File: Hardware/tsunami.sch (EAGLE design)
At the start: 154 parts, among them J1 VDC-IN, J10 TRIG2, J11 TRIG1, J12 USD-SDIO-SOCKET, J13 GND, J14 AUDIO I/O, J15 MIDI, J2 GND-IN, J3 DEBUG, J4 USB-MICROB", J5 CORTEX_DEBUGPTH, J6 3.3VA, J7 3.3V, J8 !PLAYING, J9 FTDI_DEVICE, Q1 2.5A/30V, U1 LM1117, U2 LM1117, U3 ATSAMS70NXXA-AN, U4 AK4618VQSFE-PACKAGE, U5 74AHC1G125, U6 6N138M, Y1 11.2896 MHz

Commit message: Updates from reviews.
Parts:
- added TP5: SWDIO/TMS, SparkFun-Passives:TEST-POINTTP_15TH_THRU
- added TP6: SWCK/TCK, SparkFun-Passives:TEST-POINTTP_15TH_THRU
- added TP7: TDO, SparkFun-Passives:TEST-POINTTP_15TH_THRU
- added TP8: TDI, SparkFun-Passives:TEST-POINTTP_15TH_THRU
- added TP9: NRESET, SparkFun-Passives:TEST-POINTTP_15TH_THRU
- U3: value ATSAMS70NXXA-AN -> ATSAMS70N20A-AN
- renumbered L2 to FB1, L3 to FB2, L4 to FB3
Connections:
- net 3.3V_A renamed VCCA
- net N$7 renamed VBUS
- new net SHIELD: J4.SHIELD
- net NRESET: now also TP9.1
- net SWCLK/TCK: now also TP6.1
- net SWDIO/TMS: now also TP5.1
- net TDI: now also TP8.1
- net TDO: now also TP7.1
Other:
- note added: "Highpass filters with 1.59 Hz cutoff."
- note added: "Lowpass filters with 159 kHz cutoff."
- note added: "Power inputs prioritize header over USB. If 5V is present on both, current is drawn from header."
- note removed: "Power inputs prioritize header over USB. If 5V is present on both, current is drawn from barrel."
- moved on the sheet: D1, J3, J4, J5, R10, R5, R6, R9

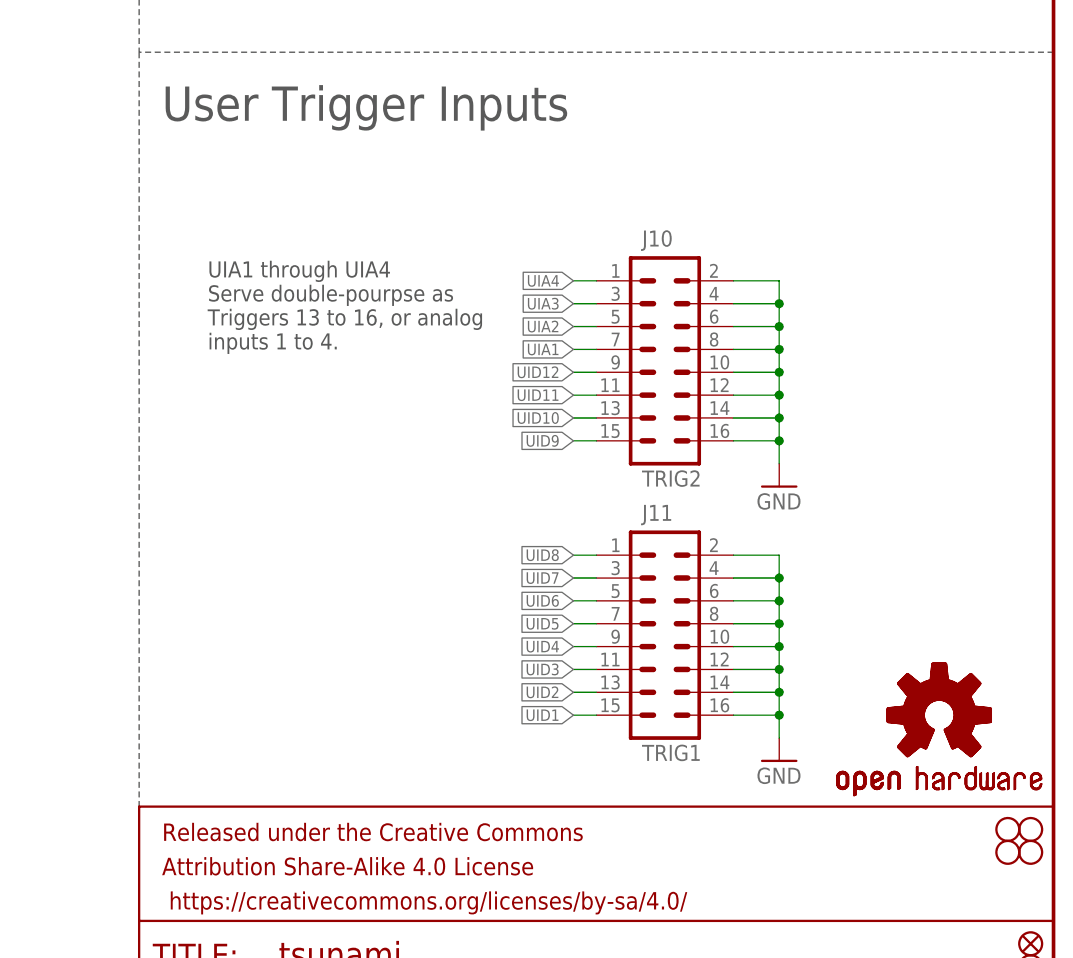
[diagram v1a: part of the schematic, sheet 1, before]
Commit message: Some checklist touchups
JTAG TP's placed on 50 mil grid.
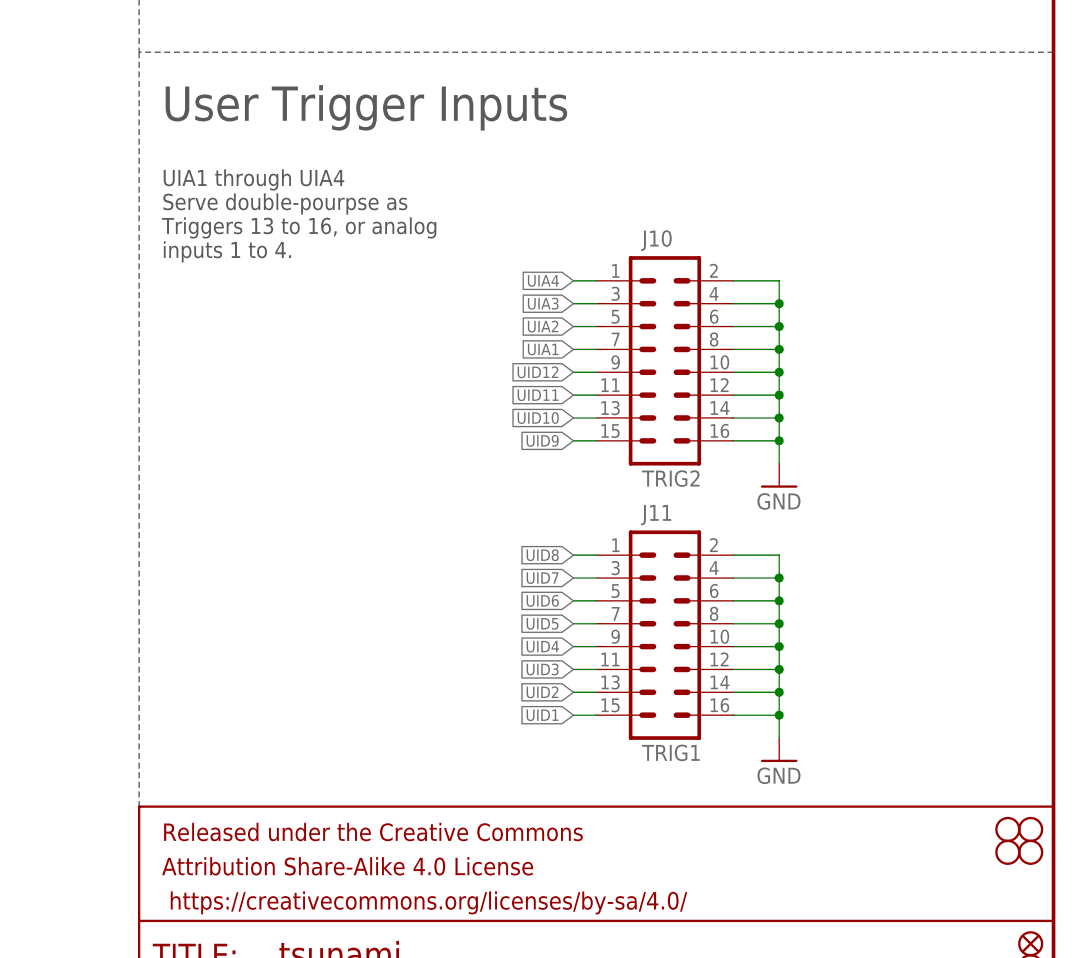
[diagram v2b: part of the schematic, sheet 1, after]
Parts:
- removed LOGO2, LOGO3: OSHW-LOGOM, SparkFun-Aesthetics:OSHW-LOGOM
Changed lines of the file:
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@@
 <part name="FD1" library="SparkFun-Aesthetics" deviceset="FIDUCIAL" device="UFIDUCIAL"/>
 <part name="FD2" library="SparkFun-Aesthetics" deviceset="FIDUCIAL" device="UFIDUCIAL"/>
-<part name="LOGO3" library="SparkFun-Aesthetics" deviceset="OSHW-LOGO" device="M"/>
 <part name="LOGO1" library="SparkFun-Aesthetics" deviceset="SFE_LOGO_NAME" device=".2_INCH"/>
 <part name="Q1" library="SparkFun-DiscreteSemi" deviceset="MOSFET-PCHANNEL" device="DMG2307L" value="2.5A/30V"/>
@@
 <part name="J1" library="SparkFun-Connectors" deviceset="M02" device="PTH" value="VDC-IN"/>
 <part name="J2" library="SparkFun-Connectors" deviceset="M02" device="PTH" value="GND-IN"/>
-<part name="LOGO2" library="SparkFun-Aesthetics" deviceset="OSHW-LOGO" device="M"/>
 <part name="U$1" library="SparkFun-Aesthetics" deviceset="VCCA" device=""/>
 <part name="U$2" library="SparkFun-Aesthetics" deviceset="VCCA" device=""/>
@@
 <wire x1="63.5" y1="58.42" x2="119.38" y2="58.42" width="0.1524" layer="97" style="shortdash"/>
 <wire x1="330.2" y1="279.4" x2="330.2" y2="215.9" width="0.1524" layer="97" style="shortdash"/>
-<text x="337.82" y="86.36" size="1.778" layer="97" font="vector">UIA1 through UIA4
+<text x="332.74" y="96.52" size="1.778" layer="97" font="vector">UIA1 through UIA4
 Serve double-pourpse as
 Triggers 13 to 16, or analog
@@
 <instance part="FD1" gate="G$1" x="429.26" y="20.32"/>
 <instance part="FD2" gate="G$1" x="429.26" y="17.78"/>
-<instance part="LOGO3" gate="G$1" x="419.1" y="45.72"/>
 <instance part="LOGO1" gate="G$1" x="273.05" y="0.508"/>
 <instance part="Q1" gate="G$1" x="38.1" y="238.76" rot="R90"/>
@@
 <instance part="J1" gate="G$1" x="7.62" y="246.38"/>
 <instance part="J2" gate="G$1" x="7.62" y="228.6"/>
-<instance part="LOGO2" gate="G$1" x="419.1" y="45.72"/>
 <instance part="U$1" gate="G$1" x="101.6" y="271.78"/>
 <instance part="TP5" gate="G$1" x="73.66" y="40.64" rot="R90"/>

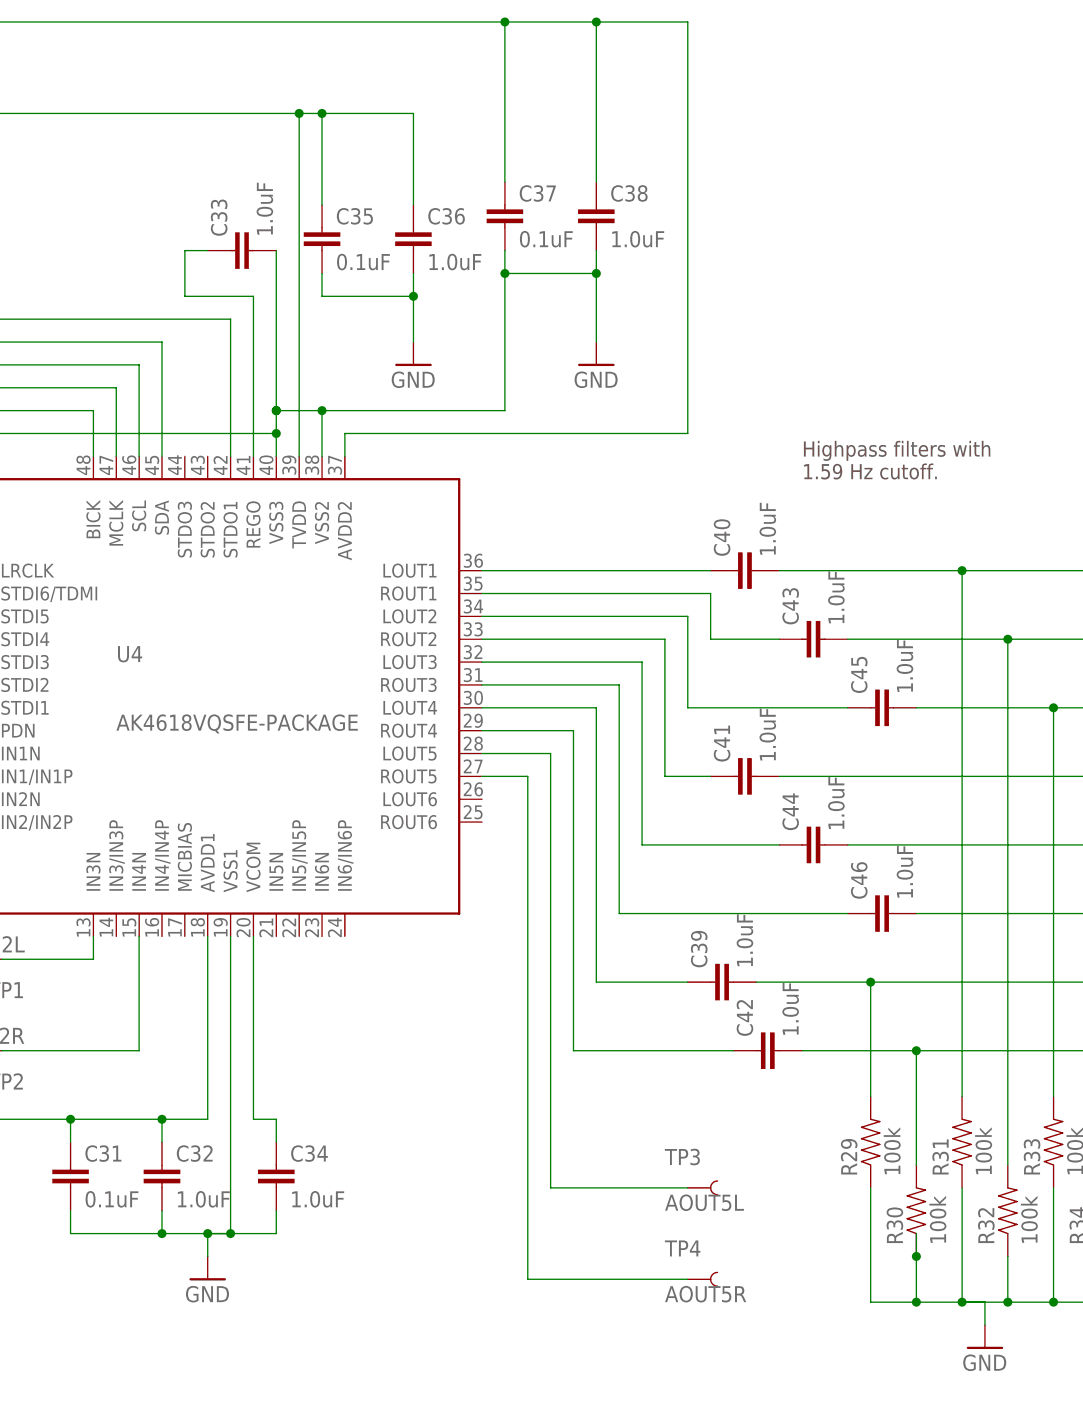
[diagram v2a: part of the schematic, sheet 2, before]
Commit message: Addressing Eric's punch list.
See issue #2
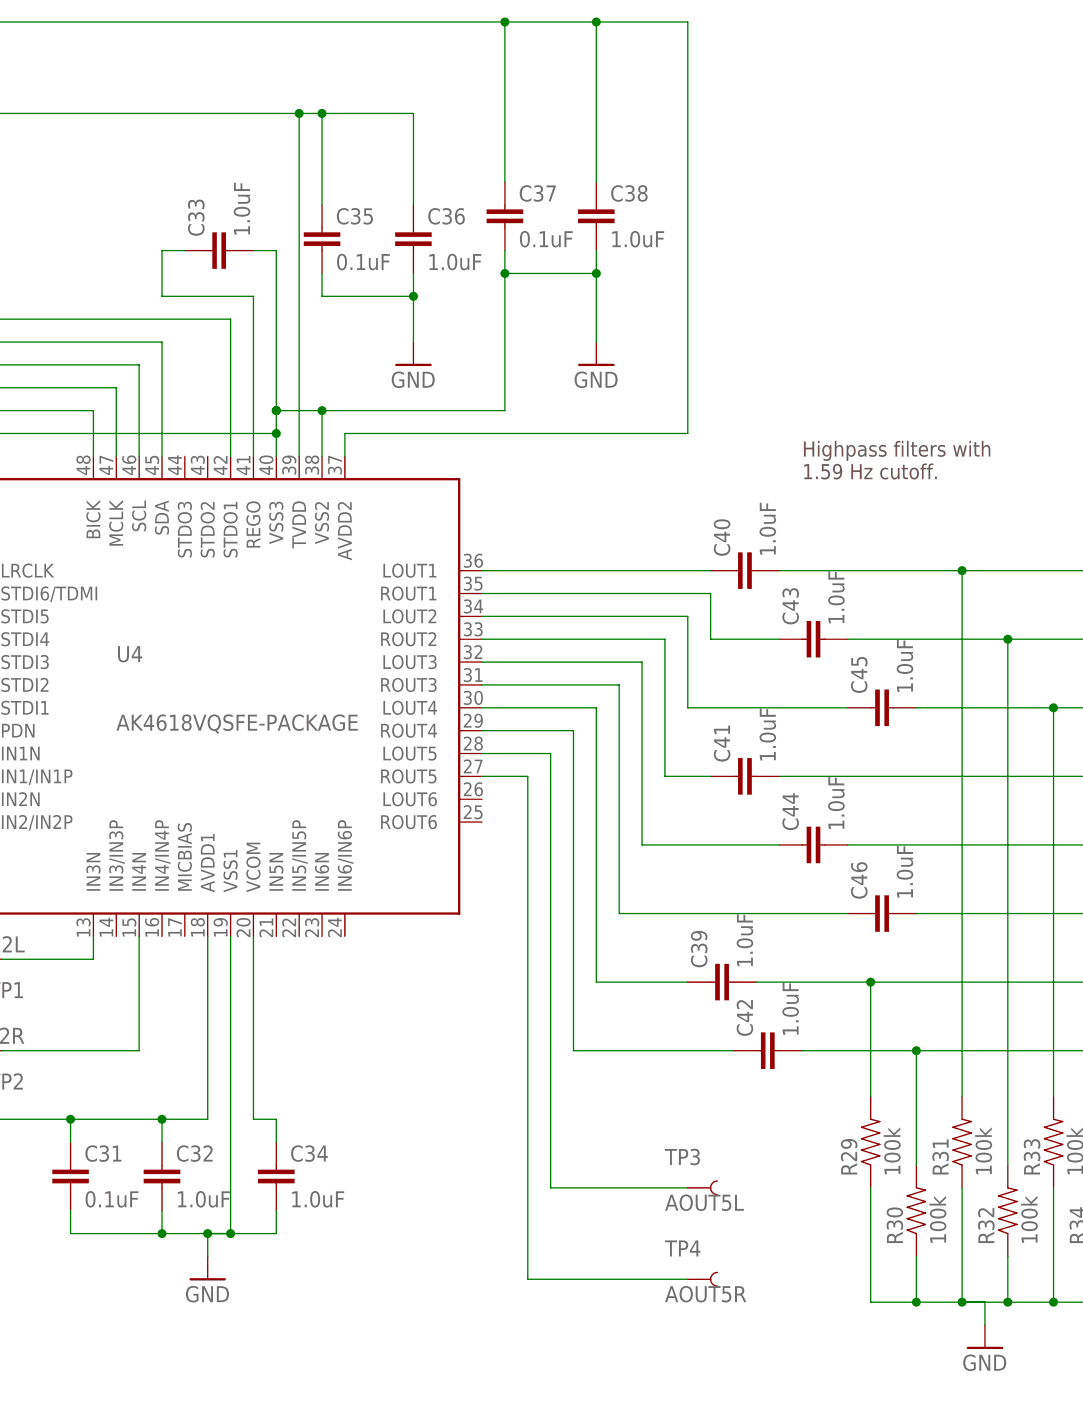
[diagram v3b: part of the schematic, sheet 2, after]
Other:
- moved on the sheet: C33

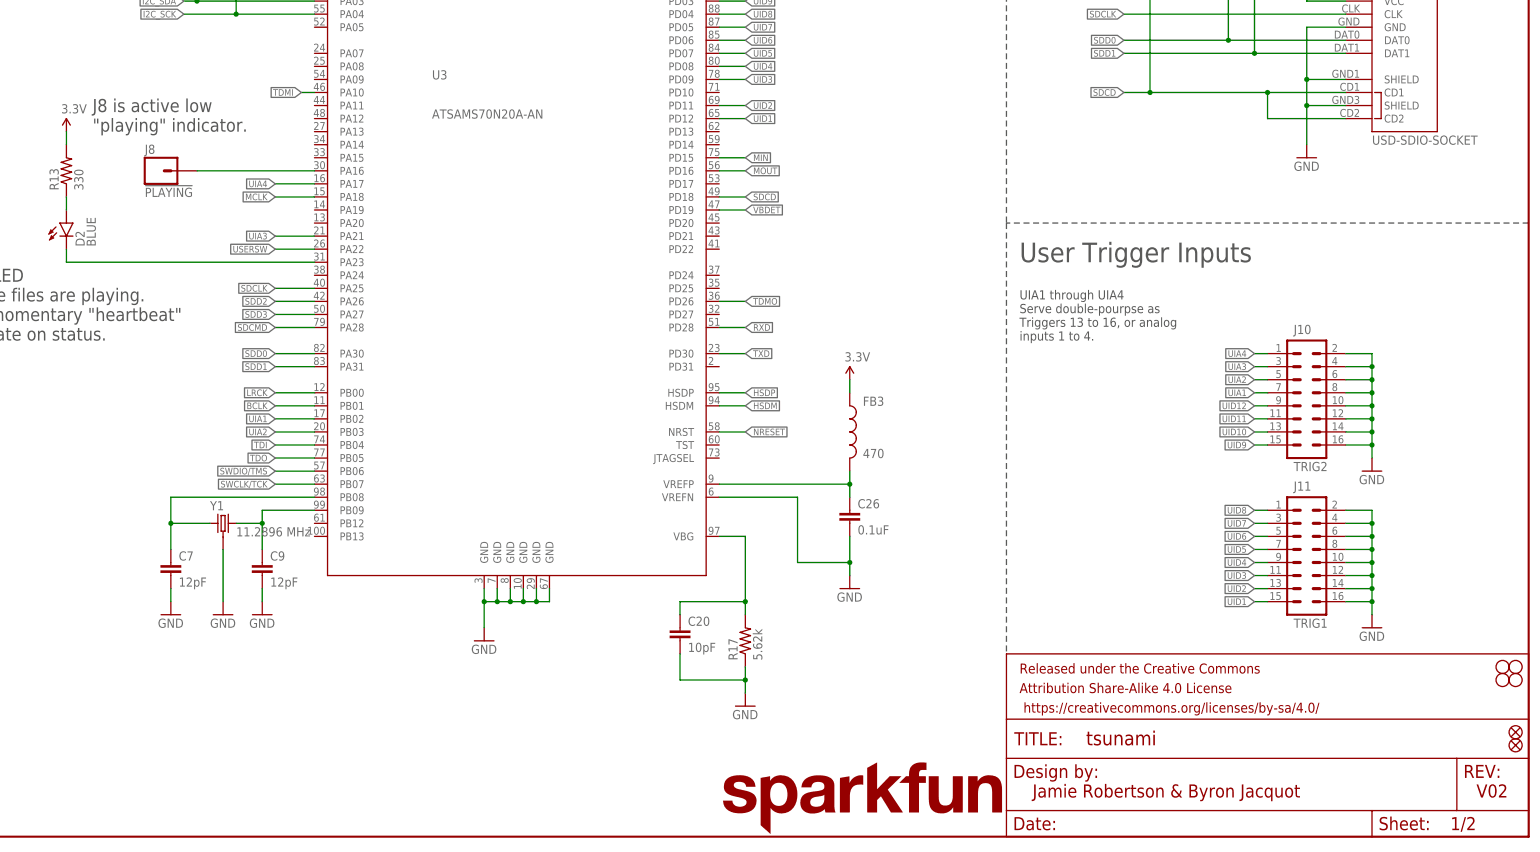
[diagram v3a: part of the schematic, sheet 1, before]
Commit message: Updates for production.
Silkscreen touchups.
-all silk on back is right side up.
-some size & placement adjustments to labels.  Name is larger, some pad
labels are smaller.
-JTAG and DEBUG labels removed from both sides of board.
-Playing is active high, overbar deleted.

Only copper change is version number, rolled to ""V10."
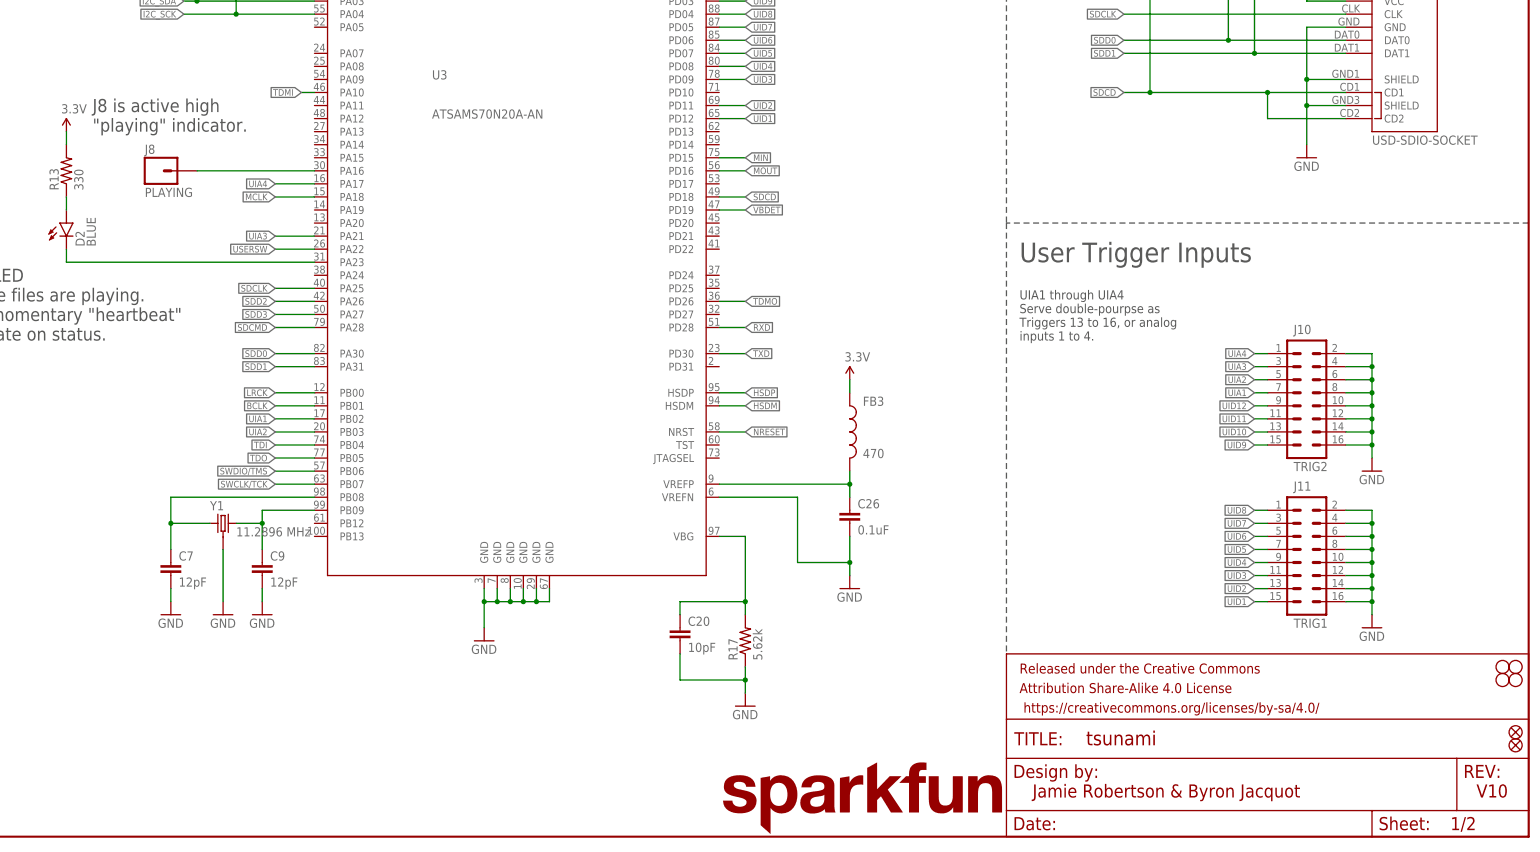
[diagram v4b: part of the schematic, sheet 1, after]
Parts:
- J8: value !PLAYING -> PLAYING
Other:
- note added: "J8 is active high "playing" indicator."
- note added: "V10"
- note removed: "J8 is active low "playing" indicator."
- note removed: "V02"
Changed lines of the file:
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@@
 <layer number="255" name="routoute" color="7" fill="1" visible="yes" active="yes"/>
 </layers>
-<schematic xreflabel="%F%N" xrefpart="/%S.%C%R">
+<schematic xreflabel="%F%N/%S" xrefpart="/%S.%C%R">
 <attributes>
 </attributes>
@@
 <part name="GND11" library="SparkFun-Aesthetics" deviceset="GND" device=""/>
 <part name="J3" library="SparkFun-Connectors" deviceset="M01" device="PTH_NO_SILK_YES_STOP" value="DEBUG"/>
-<part name="J8" library="SparkFun-Connectors" deviceset="M01" device="PTH_NO_SILK_YES_STOP" value="!PLAYING"/>
+<part name="J8" library="SparkFun-Connectors" deviceset="M01" device="PTH_NO_SILK_YES_STOP" value="PLAYING"/>
 <part name="S1" library="SparkFun-Electromechanical" deviceset="SWITCH-MOMENTARY-2" device="SMD" value="Reset"/>
 <part name="S3" library="SparkFun-Electromechanical" deviceset="SWITCH-MOMENTARY-2" device="SMD" value="User"/>
@@
 <wire x1="431.8" y1="119.38" x2="330.2" y2="119.38" width="0.1524" layer="97" style="shortdash"/>
 <text x="335.28" y="7.62" size="2.54" layer="94" font="vector">Jamie Robertson &amp; Byron Jacquot</text>
-<text x="421.64" y="7.62" size="2.54" layer="94" font="vector">V02</text>
+<text x="421.64" y="7.62" size="2.54" layer="94" font="vector">V10</text>
 <text x="249.428" y="236.728" size="1.778" layer="97">Near each VDDCORE pin</text>
 <text x="216.408" y="236.728" size="1.778" layer="97">Near each VDDIO pin</text>
@@
 <wire x1="63.5" y1="58.42" x2="63.5" y2="104.14" width="0.1524" layer="97" style="shortdash"/>
 <text x="66.04" y="96.52" size="3.81" layer="97" font="vector">User Switch</text>
-<text x="152.4" y="137.16" size="2.54" layer="97" font="vector">J8 is active low
+<text x="152.4" y="137.16" size="2.54" layer="97" font="vector">J8 is active high
 "playing" indicator.</text>
 <text x="68.58" y="60.96" size="1.778" layer="97">S4 is optional, side-firing 6mm tact type.</text>
@@
 <text x="347.98" y="185.42" size="5.08" layer="97" font="vector">MIDI OUT</text>
 <text x="335.28" y="7.62" size="2.54" layer="94" font="vector">Jamie Robertson &amp; Byron Jacquot</text>
-<text x="421.64" y="7.62" size="2.54" layer="94" font="vector">V02</text>
+<text x="421.64" y="7.62" size="2.54" layer="94" font="vector">V10</text>
 <wire x1="330.2" y1="279.4" x2="330.2" y2="198.12" width="0.1524" layer="97" style="shortdash"/>
 <wire x1="330.2" y1="198.12" x2="330.2" y2="127" width="0.1524" layer="97" style="shortdash"/>
